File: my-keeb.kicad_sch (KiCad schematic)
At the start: 6 parts

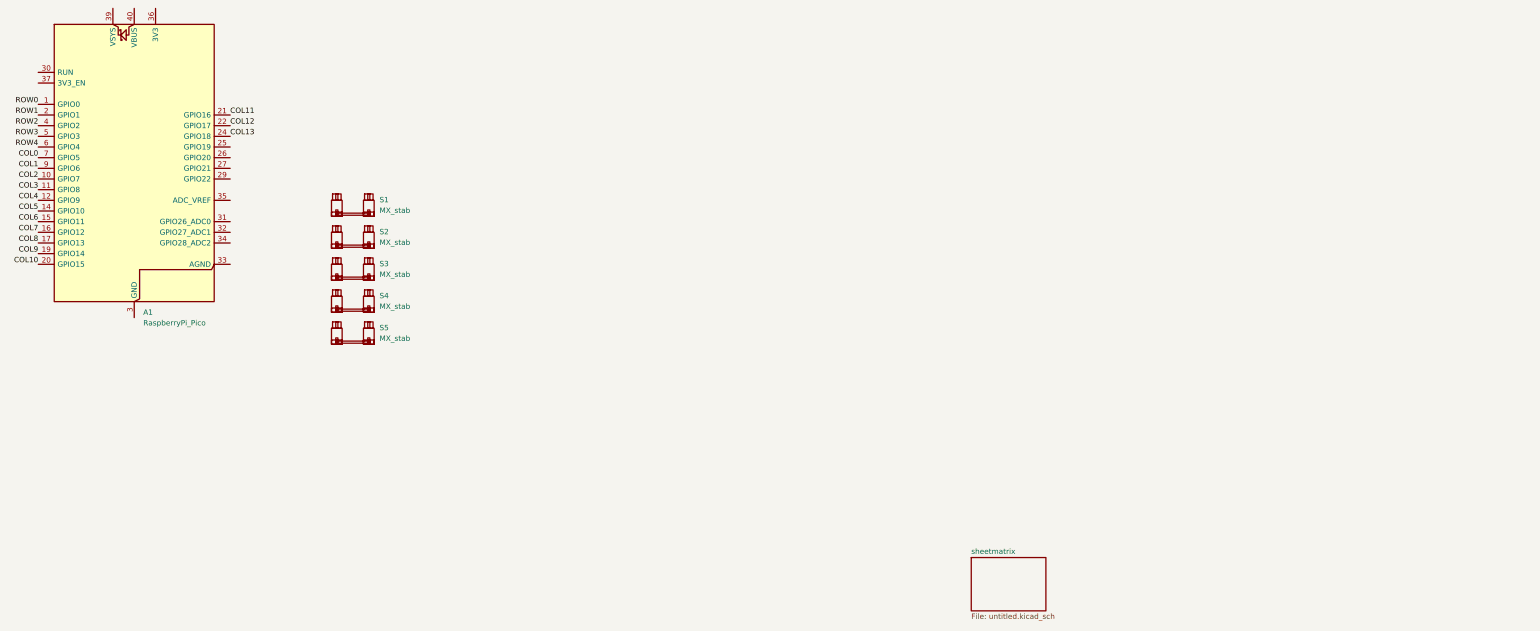
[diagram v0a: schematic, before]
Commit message: FIXES
im never using a matrix sheet
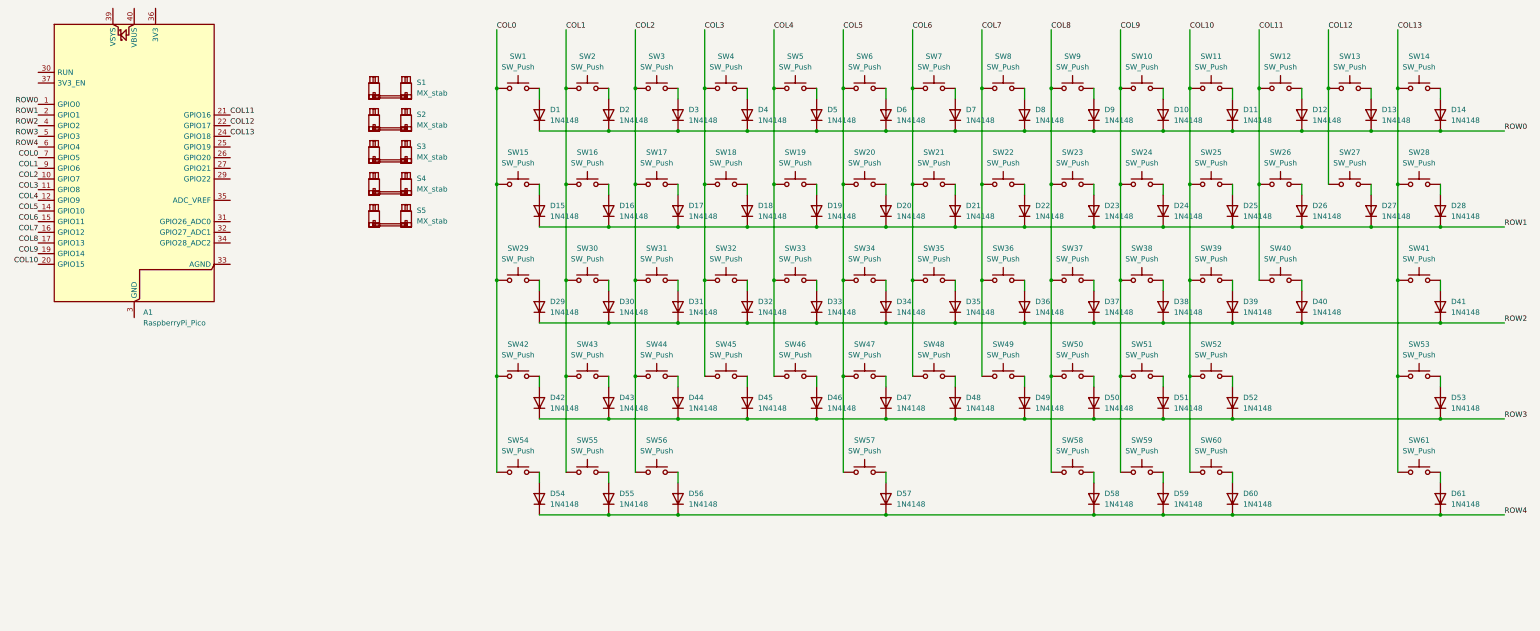
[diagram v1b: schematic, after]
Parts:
- added D1, D10, D11, D12, D13, D14, D15, D16, D17, D18, D19, D2, D20, D21, D22, D23, D24, D25, D26, D27, D28, D29, D3, D30, D31, D32, D33, D34, D35, D36, D37, D38, D39, D4, D40, D41, D42, D43, D44, D45, D46, D47, D48, D49, D5, D50, D51, D52, D53, D54, D55, D56, D57, D58, D59, D6, D60, D61, D7, D8, D9: 1N4148, Diode_THT:D_DO-35_SOD27_P7.62mm_Horizontal, symbol Diode:1N4148
- added SW1, SW10, SW11, SW12, SW13, SW14, SW16, SW17, SW18, SW19, SW2, SW20, SW21, SW22, SW23, SW24, SW25, SW26, SW27, SW3, SW30, SW31, SW32, SW33, SW34, SW35, SW36, SW37, SW38, SW39, SW4, SW40, SW41, SW42, SW43, SW44, SW45, SW46, SW47, SW48, SW49, SW5, SW50, SW51, SW52, SW53, SW57, SW6, SW7, SW8, SW9: SW_Push, PCM_marbastlib-mx:SW_MX_1u, symbol Switch:SW_Push
- added SW15, SW28: SW_Push, PCM_marbastlib-mx:SW_MX_1.5u, symbol Switch:SW_Push
- added SW29: SW_Push, PCM_marbastlib-mx:SW_MX_1.75u, symbol Switch:SW_Push
- added SW54, SW55, SW56, SW58, SW59, SW60, SW61: SW_Push, PCM_marbastlib-mx:SW_MX_1.25u, symbol Switch:SW_Push
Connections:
- net COL0: now also SW1.1, SW15.1, SW29.1, SW42.1, SW54.1
- net COL1: now also SW16.1, SW2.1, SW30.1, SW43.1, SW55.1
- net COL10: now also SW11.1, SW25.1, SW39.1, SW52.1, SW60.1
- net COL11: now also SW12.1, SW26.1, SW40.1
- net COL12: now also SW13.1, SW27.1
- net COL13: now also SW14.1, SW28.1, SW41.1, SW53.1, SW61.1
- net COL2: now also SW17.1, SW3.1, SW31.1, SW44.1, SW56.1
- net COL3: now also SW18.1, SW32.1, SW4.1, SW45.1
- net COL4: now also SW19.1, SW33.1, SW46.1, SW5.1
- net COL5: now also SW20.1, SW34.1, SW47.1, SW57.1, SW6.1
- net COL6: now also SW21.1, SW35.1, SW48.1, SW7.1
- net COL7: now also SW22.1, SW36.1, SW49.1, SW8.1
- net COL8: now also SW23.1, SW37.1, SW50.1, SW58.1, SW9.1
- net COL9: now also SW10.1, SW24.1, SW38.1, SW51.1, SW59.1
- net ROW0: now also D1.1 (K), D10.1 (K), D11.1 (K), D12.1 (K), D13.1 (K), D14.1 (K), D2.1 (K), D3.1 (K), D4.1 (K), D5.1 (K), D6.1 (K), D7.1 (K), D8.1 (K), D9.1 (K)
- net ROW1: now also D15.1 (K), D16.1 (K), D17.1 (K), D18.1 (K), D19.1 (K), D20.1 (K), D21.1 (K), D22.1 (K), D23.1 (K), D24.1 (K), D25.1 (K), D26.1 (K), D27.1 (K), D28.1 (K)
- net ROW2: now also D29.1 (K), D30.1 (K), D31.1 (K), D32.1 (K), D33.1 (K), D34.1 (K), D35.1 (K), D36.1 (K), D37.1 (K), D38.1 (K), D39.1 (K), D40.1 (K), D41.1 (K)
- net ROW3: now also D42.1 (K), D43.1 (K), D44.1 (K), D45.1 (K), D46.1 (K), D47.1 (K), D48.1 (K), D49.1 (K), D50.1 (K), D51.1 (K), D52.1 (K), D53.1 (K)
- net ROW4: now also D54.1 (K), D55.1 (K), D56.1 (K), D57.1 (K), D58.1 (K), D59.1 (K), D60.1 (K), D61.1 (K)
- new net: D29.2 (A), SW29.2
- new net: D34.2 (A), SW34.2
- new net: D37.2 (A), SW37.2
- new net: D11.2 (A), SW11.2
- new net: D61.2 (A), SW61.2
- new net: D42.2 (A), SW42.2
- new net: D10.2 (A), SW10.2
- new net: D38.2 (A), SW38.2
- new net: D48.2 (A), SW48.2
- new net: D53.2 (A), SW53.2
- new net: D58.2 (A), SW58.2
- new net: D22.2 (A), SW22.2
- new net: D2.2 (A), SW2.2
- new net: D26.2 (A), SW26.2
- new net: D49.2 (A), SW49.2
- new net: D13.2 (A), SW13.2
- new net: D43.2 (A), SW43.2
- new net: D16.2 (A), SW16.2
- new net: D24.2 (A), SW24.2
- new net: D39.2 (A), SW39.2
- new net: D28.2 (A), SW28.2
- new net: D23.2 (A), SW23.2
- new net: D27.2 (A), SW27.2
- new net: D7.2 (A), SW7.2
- new net: D60.2 (A), SW60.2
- new net: D20.2 (A), SW20.2
- new net: D25.2 (A), SW25.2
- new net: D4.2 (A), SW4.2
- new net: D57.2 (A), SW57.2
- new net: D52.2 (A), SW52.2
- new net: D31.2 (A), SW31.2
- new net: D3.2 (A), SW3.2
- new net: D46.2 (A), SW46.2
- new net: D8.2 (A), SW8.2
- new net: D55.2 (A), SW55.2
- new net: D56.2 (A), SW56.2
- new net: D17.2 (A), SW17.2
- new net: D32.2 (A), SW32.2
- new net: D47.2 (A), SW47.2
- new net: D14.2 (A), SW14.2
- new net: D59.2 (A), SW59.2
- new net: D21.2 (A), SW21.2
- new net: D41.2 (A), SW41.2
- new net: D5.2 (A), SW5.2
- new net: D36.2 (A), SW36.2
- new net: D50.2 (A), SW50.2
- new net: D45.2 (A), SW45.2
- new net: D33.2 (A), SW33.2
- new net: D30.2 (A), SW30.2
- new net: D54.2 (A), SW54.2
- new net: D44.2 (A), SW44.2
- new net: D51.2 (A), SW51.2
- new net: D12.2 (A), SW12.2
- new net: D40.2 (A), SW40.2
- new net: D6.2 (A), SW6.2
- new net: D1.2 (A), SW1.2
- new net: D35.2 (A), SW35.2
- new net: D18.2 (A), SW18.2
- new net: D19.2 (A), SW19.2
- new net: D15.2 (A), SW15.2
- new net: D9.2 (A), SW9.2
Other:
- removed sheet sheetmatrix
- moved on the sheet: S1, S2, S3, S4, S5
